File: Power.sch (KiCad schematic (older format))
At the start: 32 parts, among them J14 Conn_01x02, Q5 AO3401A, U3 TPS54228, U4 TPS54228

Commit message: Finished revising power section schematic
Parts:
- removed C10, C9: 1u, Capacitor_SMD:C_0603_1608Metric, symbol Device:C
- removed C11, C12: 3n3, Capacitor_SMD:C_0603_1608Metric, symbol Device:C
- removed C13, C14: 100n, Capacitor_SMD:C_0603_1608Metric, symbol Device:C
- removed C15, C16, C17, C18: 22u, Capacitor_SMD:C_0805_2012Metric, symbol Device:C
- removed C5, C7, C8: 10u, Capacitor_SMD:C_0805_2012Metric, symbol Device:C
- removed L1: 3u3, co2_sensor_node:YP0403, symbol Device:L
- removed L2: 4u7, co2_sensor_node:WPN4020, symbol Device:L
- removed R10: 73k2, Resistor_SMD:R_0603_1608Metric, symbol Device:R
- removed R11, R13: 22k1, Resistor_SMD:R_0603_1608Metric, symbol Device:R
- removed R12: 165k, Resistor_SMD:R_0603_1608Metric, symbol Device:R
- removed R8, R9: 10k, Resistor_SMD:R_0603_1608Metric, symbol Device:R
- removed U3, U4: TPS54228, Package_SON:VSON-10-1EP_3x3mm_P0.5mm_EP1.2x2mm, symbol co2_sensor_node:TPS54228
- removed U?: TPS62130, Package_DFN_QFN:VQFN-16-1EP_3x3mm_P0.5mm_EP1.68x1.68mm_ThermalVias, symbol Regulator_Switching:TPS62130
- added C? (x2): 22u, symbol Device:C
- added C?: 10u, Capacitor_SMD:C_0805_2012Metric, symbol Device:C
- added C?: 100n, symbol Device:C
- added C?: 3n3, symbol Device:C
- added L? (x2): 2u2, symbol Device:L
- added R? (x2): 100k, symbol Device:R
- added R? (x2): 180k, symbol Device:R
- added R?: 562k, symbol Device:R
- added R?: 1M17, symbol Device:R
- added U?: TPS62130, Package_DFN_QFN:VQFN-16-1EP_3x3mm_P0.5mm_EP1.68x1.68mm_ThermalVias, symbol Regulator_Switching:TPS62130
- U?: LCSC (none) -> C43590
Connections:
- net labels added: +3V3
- net labels removed: +3.3V
- wire segments 124 -> 104
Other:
- note added: "13.2m ESR spec."
- note added: "3.3V Supply\n"
- note added: "VIN: 6-9 V\nVOUT: 3.3 V\nIOUT: 1.5 A\nFREQ: 1.25 MHz\nDesigned according to WEBENCH\n"
- note added: "VIN: 6-9 V\nVOUT: 6 V\nIOUT: 1 A\nFREQ: 1.25 MHz\nDesigned according to WEBENCH\n"
- note removed: "3V3 Supply\n"
- note removed: "Note: actual output is 6V5\n"
- moved on the sheet: C6, C?, D1, J14, Q5, R7, U?

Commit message: Start PCB layout
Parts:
- C10, C7, C8, C9: renamed from C?; footprint (none) -> Capacitor_SMD:C_0603_1608Metric
- C11, C12: renamed from C?; footprint (none) -> Capacitor_SMD:C_0805_2012Metric
- L1, L2: renamed from L?; footprint (none) -> co2_sensor_node:WPN4020; LCSC (none) -> C98361
- R10, R11, R12, R13, R8, R9: renamed from R?; footprint (none) -> Resistor_SMD:R_0603_1608Metric
- gave numbers to parts that had none: 3
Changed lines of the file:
@@
 	2450 2050 2500 2050
 $Comp
-L Regulator_Switching:TPS62130 U?
+L Regulator_Switching:TPS62130 U4
 U 1 1 60AE4642
 P 6100 4850
-F 0 "U?" H 6100 5531 50  0000 C CNN
+F 0 "U4" H 6100 5531 50  0000 C CNN
 F 1 "TPS62130" H 6100 5440 50  0000 C CNN
 F 2 "Package_DFN_QFN:VQFN-16-1EP_3x3mm_P0.5mm_EP1.68x1.68mm_ThermalVias" H 6250 4400 50  0001 L CNN
@@
 $EndComp
 $Comp
-L Device:C C?
+L Device:C C8
 U 1 1 60B247FC
 P 4900 4550
-F 0 "C?" H 5015 4596 50  0000 L CNN
+F 0 "C8" H 5015 4596 50  0000 L CNN
 F 1 "100n" H 5015 4505 50  0000 L CNN
-F 2 "" H 4938 4400 50  0001 C CNN
+F 2 "Capacitor_SMD:C_0603_1608Metric" H 4938 4400 50  0001 C CNN
 F 3 "~" H 4900 4550 50  0001 C CNN
 	1    4900 4550
@@
 	4900 4400 4900 4300
 $Comp
-L Device:C C?
+L Device:C C10
 U 1 1 60B5E517
 P 5250 5000
-F 0 "C?" H 5365 5046 50  0000 L CNN
+F 0 "C10" H 5365 5046 50  0000 L CNN
 F 1 "3n3" H 5365 4955 50  0000 L CNN
-F 2 "" H 5288 4850 50  0001 C CNN
+F 2 "Capacitor_SMD:C_0603_1608Metric" H 5288 4850 50  0001 C CNN
 F 3 "~" H 5250 5000 50  0001 C CNN
 	1    5250 5000
@@
 	5250 4850 5250 4750
 $Comp
-L Device:R R?
+L Device:R R13
 U 1 1 60B32241
 P 7200 5300
-F 0 "R?" H 7270 5346 50  0000 L CNN
+F 0 "R13" H 7270 5346 50  0000 L CNN
 F 1 "180k" H 7270 5255 50  0000 L CNN
-F 2 "" V 7130 5300 50  0001 C CNN
+F 2 "Resistor_SMD:R_0603_1608Metric" V 7130 5300 50  0001 C CNN
 F 3 "~" H 7200 5300 50  0001 C CNN
 	1    7200 5300
@@
 $EndComp
 $Comp
-L Device:R R?
+L Device:R R12
 U 1 1 60B341E6
 P 7200 4800
-F 0 "R?" H 7270 4846 50  0000 L CNN
+F 0 "R12" H 7270 4846 50  0000 L CNN
 F 1 "562k" H 7270 4755 50  0000 L CNN
-F 2 "" V 7130 4800 50  0001 C CNN
+F 2 "Resistor_SMD:R_0603_1608Metric" V 7130 4800 50  0001 C CNN
 F 3 "~" H 7200 4800 50  0001 C CNN
 	1    7200 4800
@@
 $EndComp
 $Comp
-L Device:L L?
+L Device:L L2
 U 1 1 60B35170
 P 6750 4650
-F 0 "L?" V 6940 4650 50  0000 C CNN
+F 0 "L2" V 6940 4650 50  0000 C CNN
 F 1 "2u2" V 6849 4650 50  0000 C CNN
-F 2 "" H 6750 4650 50  0001 C CNN
+F 2 "co2_sensor_node:WPN4020" H 6750 4650 50  0001 C CNN
 F 3 "~" H 6750 4650 50  0001 C CNN
+F 4 "C98361" V 6750 4650 50  0001 C CNN "LCSC"
 	1    6750 4650
 	0    -1   -1   0
 $EndComp
 $Comp
-L Device:C C?
+L Device:C C12
 U 1 1 60B368E2
 P 7600 4900
-F 0 "C?" H 7715 4946 50  0000 L CNN
+F 0 "C12" H 7715 4946 50  0000 L CNN
 F 1 "22u" H 7715 4855 50  0000 L CNN
-F 2 "" H 7638 4750 50  0001 C CNN
+F 2 "Capacitor_SMD:C_0805_2012Metric" H 7638 4750 50  0001 C CNN
 F 3 "~" H 7600 4900 50  0001 C CNN
 	1    7600 4900
@@
 	5250 5250 5250 5150
 $Comp
-L Device:R R?
+L Device:R R9
 U 1 1 60B2C74D
 P 6750 4950
-F 0 "R?" V 7000 4950 50  0000 C CNN
+F 0 "R9" V 7000 4950 50  0000 C CNN
 F 1 "100k" V 6900 4950 50  0000 C CNN
-F 2 "" V 6680 4950 50  0001 C CNN
+F 2 "Resistor_SMD:R_0603_1608Metric" V 6680 4950 50  0001 C CNN
 F 3 "~" H 6750 4950 50  0001 C CNN
 	1    6750 4950
@@
 	4500 2200 4500 2100
 $Comp
-L Device:C C?
+L Device:C C5
 U 1 1 60D98E74
 P 4500 2350
-F 0 "C?" H 4615 2396 50  0000 L CNN
+F 0 "C5" H 4615 2396 50  0000 L CNN
 F 1 "10u" H 4615 2305 50  0000 L CNN
 F 2 "Capacitor_SMD:C_0805_2012Metric" H 4538 2200 50  0001 C CNN
@@
 $EndComp
 $Comp
-L Regulator_Switching:TPS62130 U?
+L Regulator_Switching:TPS62130 U3
 U 1 1 60D98E7B
 P 6100 2650
-F 0 "U?" H 6100 3331 50  0000 C CNN
+F 0 "U3" H 6100 3331 50  0000 C CNN
 F 1 "TPS62130" H 6100 3240 50  0000 C CNN
 F 2 "Package_DFN_QFN:VQFN-16-1EP_3x3mm_P0.5mm_EP1.68x1.68mm_ThermalVias" H 6250 2200 50  0001 L CNN
@@
 $EndComp
 $Comp
-L Device:C C?
+L Device:C C7
 U 1 1 60D98E81
 P 4900 2350
-F 0 "C?" H 5015 2396 50  0000 L CNN
+F 0 "C7" H 5015 2396 50  0000 L CNN
 F 1 "100n" H 5015 2305 50  0000 L CNN
-F 2 "" H 4938 2200 50  0001 C CNN
+F 2 "Capacitor_SMD:C_0603_1608Metric" H 4938 2200 50  0001 C CNN
 F 3 "~" H 4900 2350 50  0001 C CNN
 	1    4900 2350
@@
 	4900 2200 4900 2100
 $Comp
-L Device:C C?
+L Device:C C9
 U 1 1 60D98E9E
 P 5250 2800
-F 0 "C?" H 5365 2846 50  0000 L CNN
+F 0 "C9" H 5365 2846 50  0000 L CNN
 F 1 "3n3" H 5365 2755 50  0000 L CNN
-F 2 "" H 5288 2650 50  0001 C CNN
+F 2 "Capacitor_SMD:C_0603_1608Metric" H 5288 2650 50  0001 C CNN
 F 3 "~" H 5250 2800 50  0001 C CNN
 	1    5250 2800
@@
 	5250 2650 5250 2550
 $Comp
-L Device:R R?
+L Device:R R11
 U 1 1 60D98EA5
 P 7200 3100
-F 0 "R?" H 7270 3146 50  0000 L CNN
+F 0 "R11" H 7270 3146 50  0000 L CNN
 F 1 "180k" H 7270 3055 50  0000 L CNN
-F 2 "" V 7130 3100 50  0001 C CNN
+F 2 "Resistor_SMD:R_0603_1608Metric" V 7130 3100 50  0001 C CNN
 F 3 "~" H 7200 3100 50  0001 C CNN
 	1    7200 3100
@@
 $EndComp
 $Comp
-L Device:R R?
+L Device:R R10
 U 1 1 60D98EAB
 P 7200 2600
-F 0 "R?" H 7270 2646 50  0000 L CNN
+F 0 "R10" H 7270 2646 50  0000 L CNN
 F 1 "1M17" H 7270 2555 50  0000 L CNN
-F 2 "" V 7130 2600 50  0001 C CNN
+F 2 "Resistor_SMD:R_0603_1608Metric" V 7130 2600 50  0001 C CNN
 F 3 "~" H 7200 2600 50  0001 C CNN
 	1    7200 2600
@@
 $EndComp
 $Comp
-L Device:L L?
+L Device:L L1
 U 1 1 60D98EB1
 P 6750 2450
-F 0 "L?" V 6940 2450 50  0000 C CNN
+F 0 "L1" V 6940 2450 50  0000 C CNN
 F 1 "2u2" V 6849 2450 50  0000 C CNN
-F 2 "" H 6750 2450 50  0001 C CNN
+F 2 "co2_sensor_node:WPN4020" H 6750 2450 50  0001 C CNN
 F 3 "~" H 6750 2450 50  0001 C CNN
+F 4 "C98361" V 6750 2450 50  0001 C CNN "LCSC"
 	1    6750 2450
 	0    -1   -1   0
 $EndComp
 $Comp
-L Device:C C?
+L Device:C C11
 U 1 1 60D98EB7
 P 7600 2700
-F 0 "C?" H 7715 2746 50  0000 L CNN
+F 0 "C11" H 7715 2746 50  0000 L CNN
 F 1 "22u" H 7715 2655 50  0000 L CNN
-F 2 "" H 7638 2550 50  0001 C CNN
+F 2 "Capacitor_SMD:C_0805_2012Metric" H 7638 2550 50  0001 C CNN
 F 3 "~" H 7600 2700 50  0001 C CNN
 	1    7600 2700
@@
 	5250 3050 5250 2950
 $Comp
-L Device:R R?
+L Device:R R8
 U 1 1 60D98F06
 P 6750 2750
-F 0 "R?" V 7000 2750 50  0000 C CNN
+F 0 "R8" V 7000 2750 50  0000 C CNN
 F 1 "100k" V 6900 2750 50  0000 C CNN
-F 2 "" V 6680 2750 50  0001 C CNN
+F 2 "Resistor_SMD:R_0603_1608Metric" V 6680 2750 50  0001 C CNN
 F 3 "~" H 6750 2750 50  0001 C CNN
 	1    6750 2750

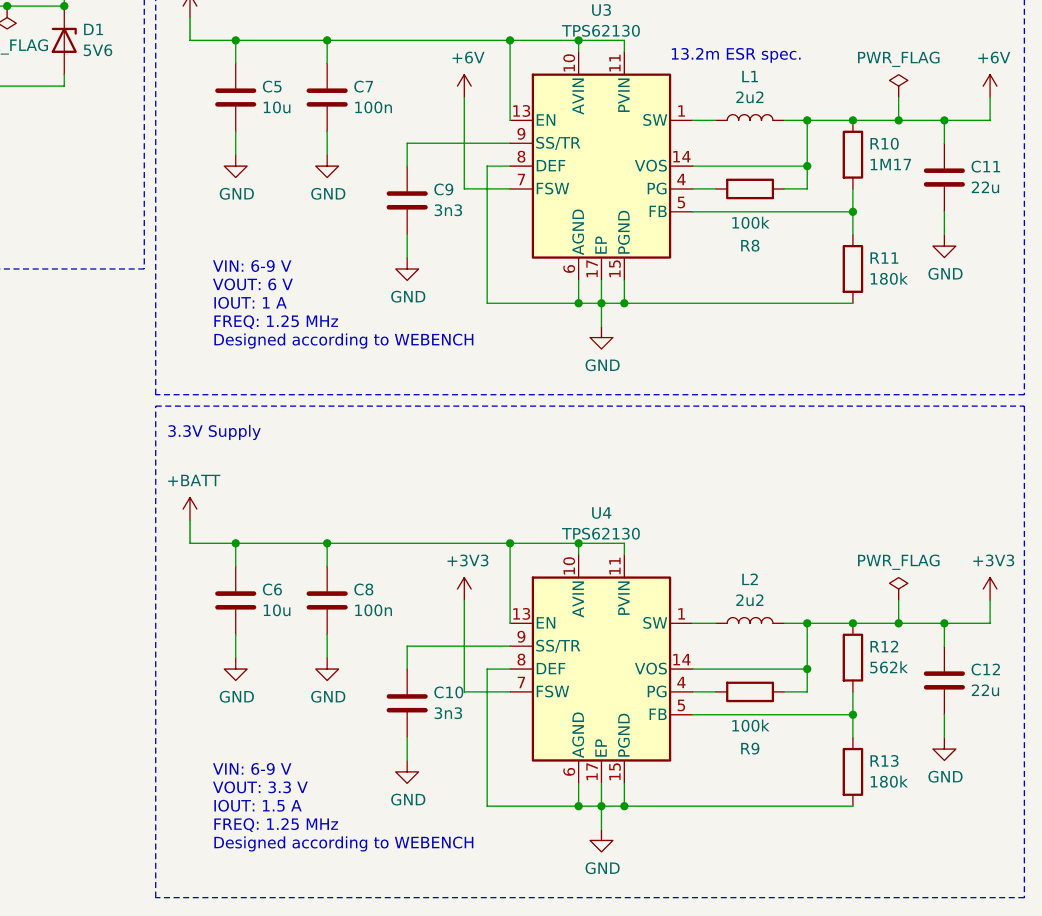
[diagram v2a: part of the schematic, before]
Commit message: First cut at layout
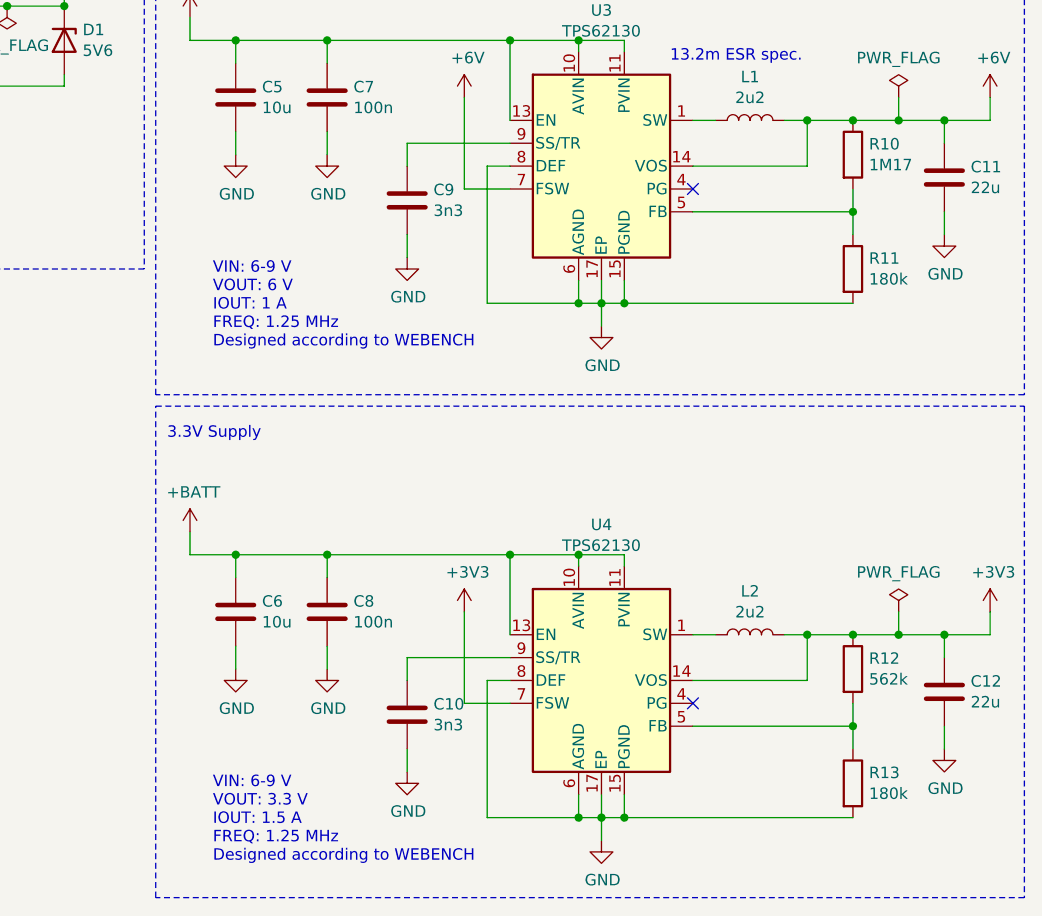
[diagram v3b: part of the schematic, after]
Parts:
- removed R8, R9: 100k, Resistor_SMD:R_0603_1608Metric, symbol Device:R
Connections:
- no-connect marks 0 -> 2
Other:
- moved on the sheet: C10, C12, C6, C8, L2, R12, R13, U4

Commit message: Export fabrication files
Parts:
- C10, C9: LCSC (none) -> C1613
- C11, C12: LCSC (none) -> C45783
- C7, C8: LCSC (none) -> C14663
- R10: LCSC (none) -> C22766
- R11, R13: LCSC (none) -> C22827
- R12: LCSC (none) -> C23205
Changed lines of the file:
@@
 F 2 "Capacitor_SMD:C_0603_1608Metric" H 4938 4450 50  0001 C CNN
 F 3 "~" H 4900 4600 50  0001 C CNN
+F 4 "C14663" H 4900 4600 50  0001 C CNN "LCSC"
 	1    4900 4600
 	1    0    0    -1
@@
 F 2 "Capacitor_SMD:C_0603_1608Metric" H 5288 4900 50  0001 C CNN
 F 3 "~" H 5250 5050 50  0001 C CNN
+F 4 "C1613" H 5250 5050 50  0001 C CNN "LCSC"
 	1    5250 5050
 	1    0    0    -1
@@
 F 2 "Resistor_SMD:R_0603_1608Metric" V 7130 5350 50  0001 C CNN
 F 3 "~" H 7200 5350 50  0001 C CNN
+F 4 "C22827" H 7200 5350 50  0001 C CNN "LCSC"
 	1    7200 5350
 	1    0    0    -1
@@
 F 2 "Resistor_SMD:R_0603_1608Metric" V 7130 4850 50  0001 C CNN
 F 3 "~" H 7200 4850 50  0001 C CNN
+F 4 "C23205" H 7200 4850 50  0001 C CNN "LCSC"
 	1    7200 4850
 	1    0    0    -1
@@
 F 2 "Capacitor_SMD:C_0805_2012Metric" H 7638 4800 50  0001 C CNN
 F 3 "~" H 7600 4950 50  0001 C CNN
+F 4 "C45783" H 7600 4950 50  0001 C CNN "LCSC"
 	1    7600 4950
 	1    0    0    -1
@@
 F 2 "Capacitor_SMD:C_0603_1608Metric" H 4938 2200 50  0001 C CNN
 F 3 "~" H 4900 2350 50  0001 C CNN
+F 4 "C14663" H 4900 2350 50  0001 C CNN "LCSC"
 	1    4900 2350
 	1    0    0    -1
@@
 F 2 "Capacitor_SMD:C_0603_1608Metric" H 5288 2650 50  0001 C CNN
 F 3 "~" H 5250 2800 50  0001 C CNN
+F 4 "C1613" H 5250 2800 50  0001 C CNN "LCSC"
 	1    5250 2800
 	1    0    0    -1
@@
 F 2 "Resistor_SMD:R_0603_1608Metric" V 7130 3100 50  0001 C CNN
 F 3 "~" H 7200 3100 50  0001 C CNN
+F 4 "C22827" H 7200 3100 50  0001 C CNN "LCSC"
 	1    7200 3100
 	1    0    0    -1
@@
 F 2 "Resistor_SMD:R_0603_1608Metric" V 7130 2600 50  0001 C CNN
 F 3 "~" H 7200 2600 50  0001 C CNN
+F 4 "C22766" H 7200 2600 50  0001 C CNN "LCSC"
 	1    7200 2600
 	1    0    0    -1
@@
 F 2 "Capacitor_SMD:C_0805_2012Metric" H 7638 2550 50  0001 C CNN
 F 3 "~" H 7600 2700 50  0001 C CNN
+F 4 "C45783" H 7600 2700 50  0001 C CNN "LCSC"
 	1    7600 2700
 	1    0    0    -1

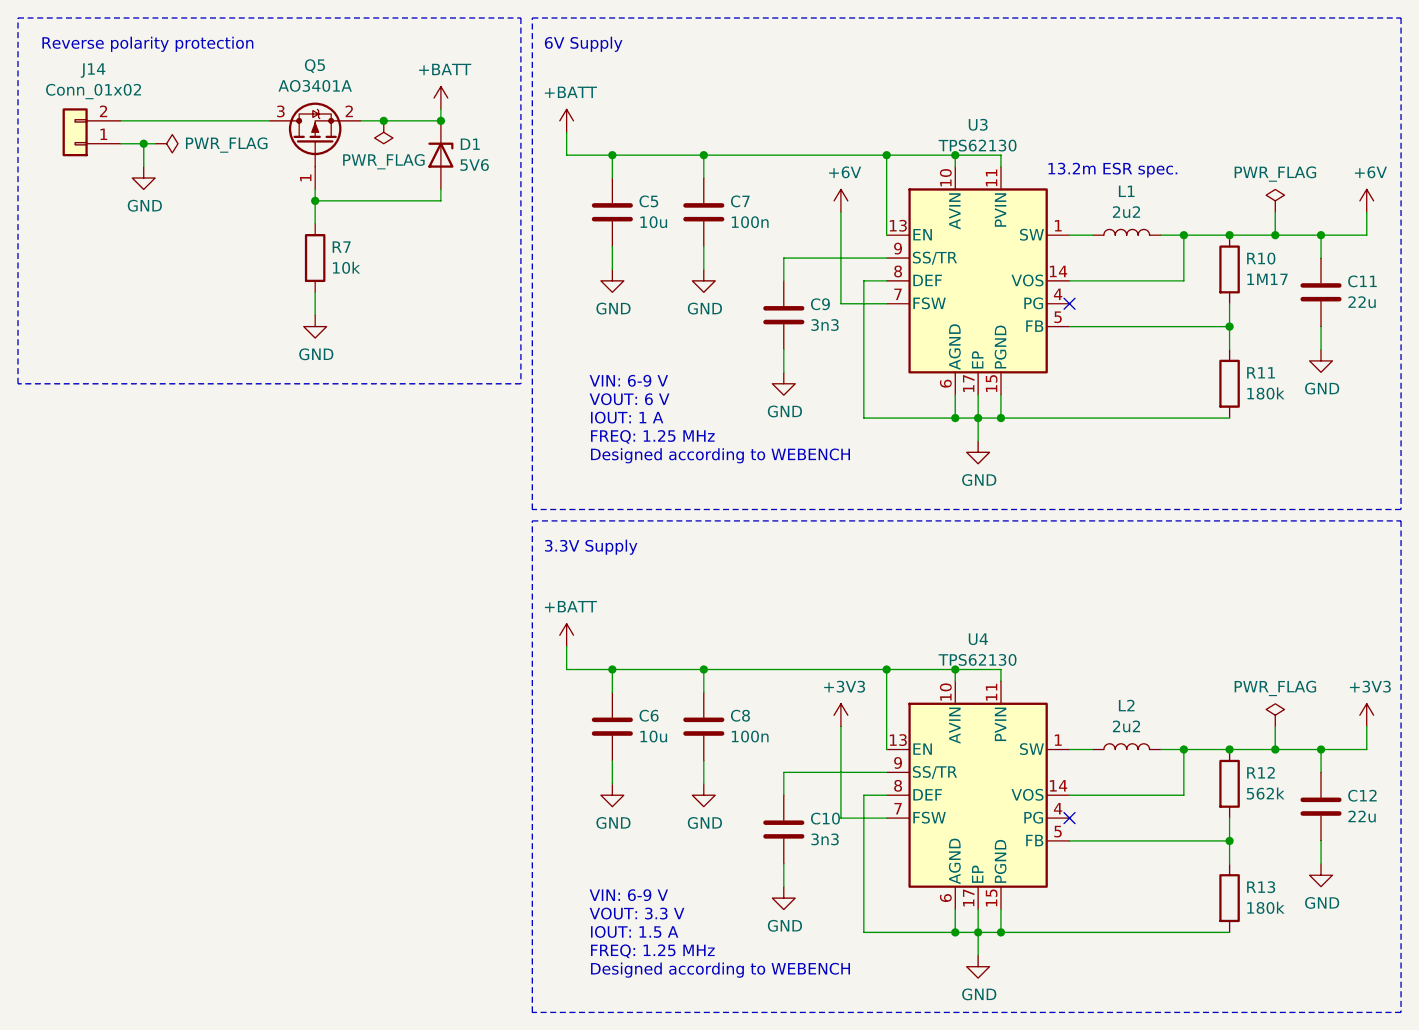
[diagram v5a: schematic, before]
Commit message: Fix sensor PMOS issue and start change to long term chamber
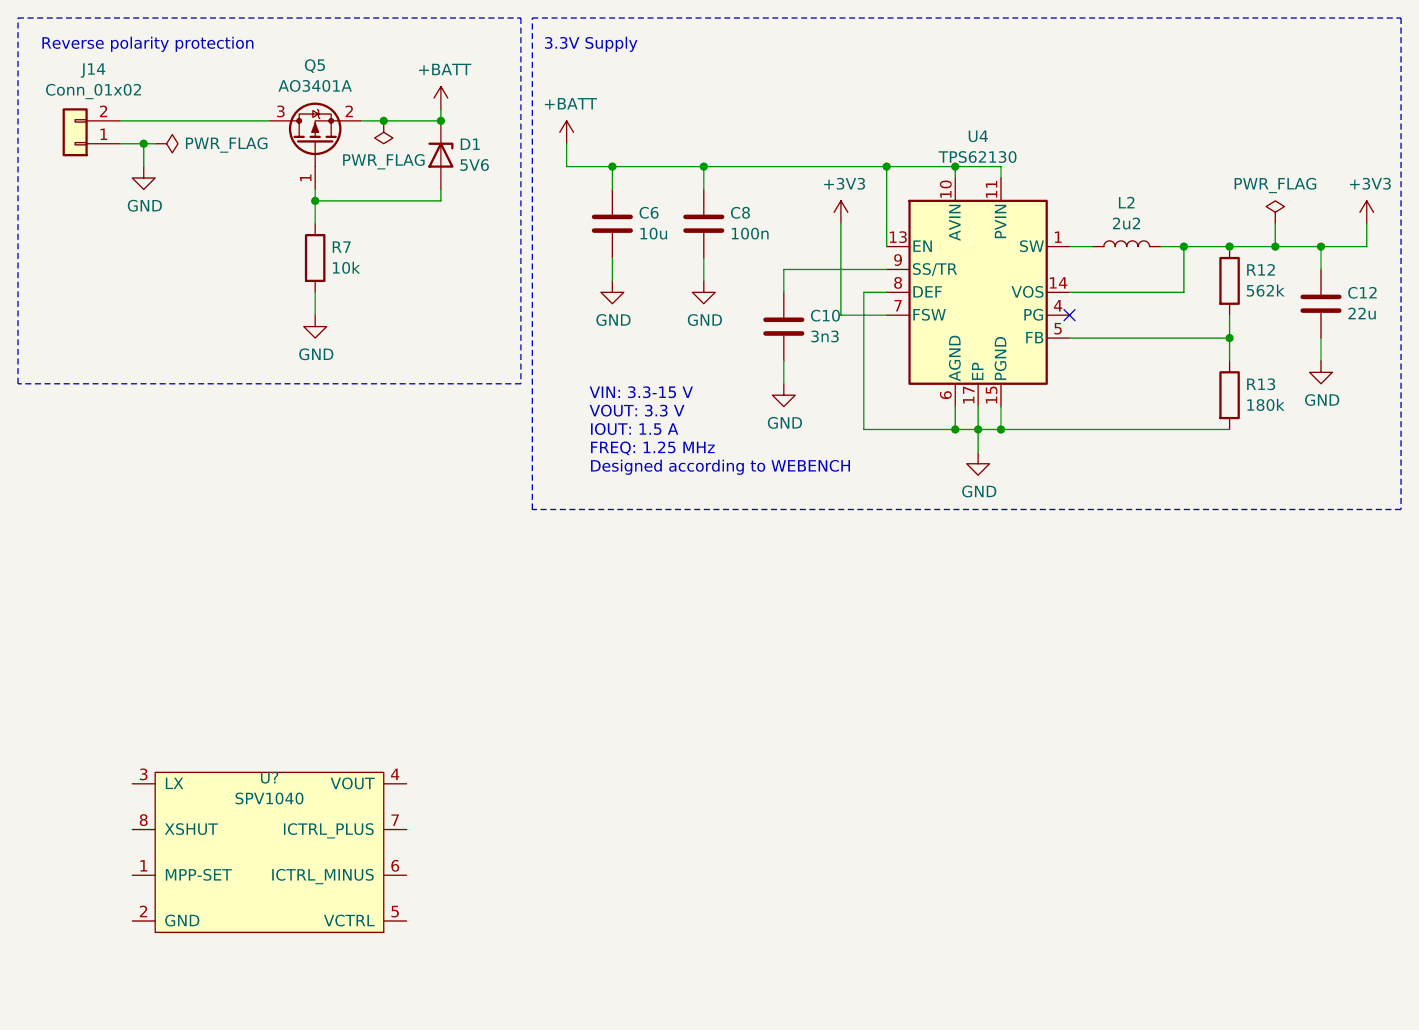
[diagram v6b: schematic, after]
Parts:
- removed C11: 22u, Capacitor_SMD:C_0805_2012Metric, symbol Device:C
- removed C5: 10u, Capacitor_SMD:C_0805_2012Metric, symbol Device:C
- removed C7: 100n, Capacitor_SMD:C_0603_1608Metric, symbol Device:C
- removed C9: 3n3, Capacitor_SMD:C_0603_1608Metric, symbol Device:C
- removed L1: 2u2, co2_sensor_node:WPN4020, symbol Device:L
- removed R10: 1M17, Resistor_SMD:R_0603_1608Metric, symbol Device:R
- removed R11: 180k, Resistor_SMD:R_0603_1608Metric, symbol Device:R
- removed U3: TPS62130, Package_DFN_QFN:VQFN-16-1EP_3x3mm_P0.5mm_EP1.68x1.68mm_ThermalVias, symbol Regulator_Switching:TPS62130
- added U?: SPV1040, Package_SO:TSSOP-8_4.4x3mm_P0.65mm, symbol co2_sensor_node:SPV1040
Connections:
- no-connect marks 2 -> 1
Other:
- note added: "VIN: 3.3-15 V\nVOUT: 3.3 V\nIOUT: 1.5 A\nFREQ: 1.25 MHz\nDesigned according to WEBENCH\n"
- note removed: "13.2m ESR spec."
- note removed: "6V Supply\n"
- note removed: "VIN: 6-9 V\nVOUT: 3.3 V\nIOUT: 1.5 A\nFREQ: 1.25 MHz\nDesigned according to WEBENCH\n"
- note removed: "VIN: 6-9 V\nVOUT: 6 V\nIOUT: 1 A\nFREQ: 1.25 MHz\nDesigned according to WEBENCH\n"
- moved on the sheet: C10, C12, C6, C8, L2, R12, R13, U4
